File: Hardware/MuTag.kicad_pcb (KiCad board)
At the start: 2 copper layers, 58.8 x 20 mm, 30 parts, among them IC1 ST25DV04K-IER6S3, J1 SPI_Header, U2 ATTiny

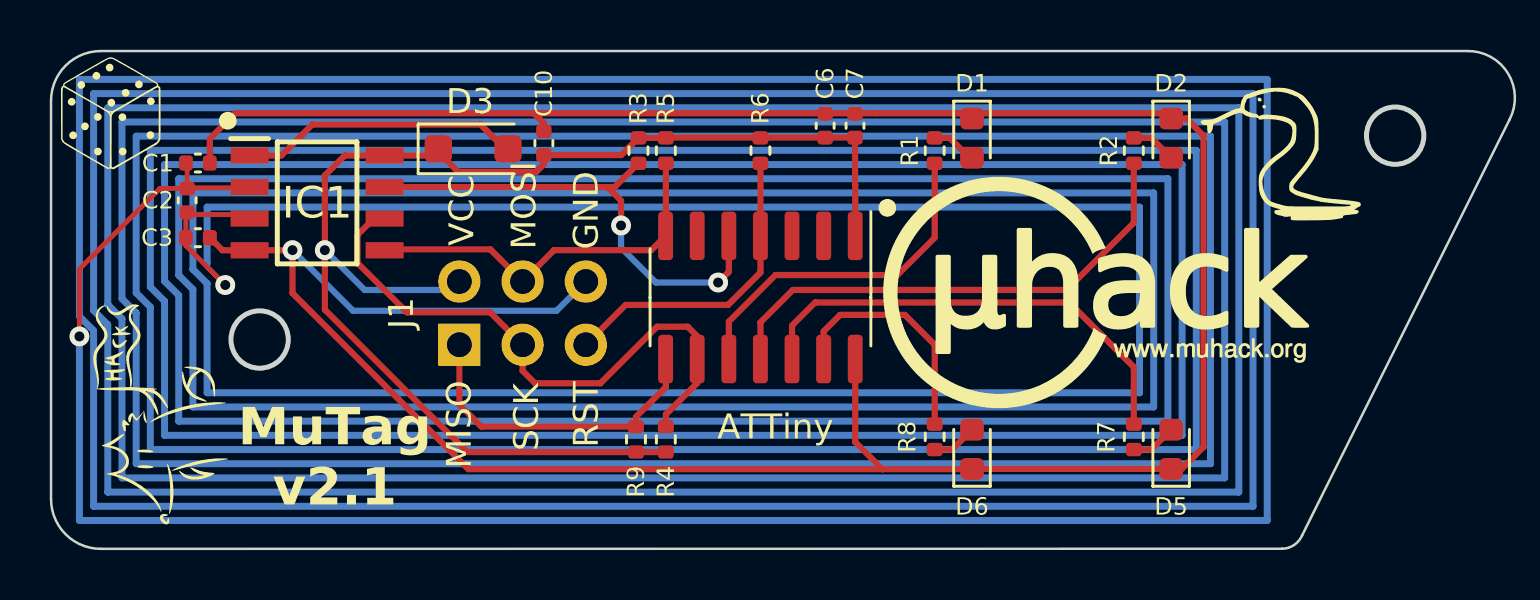
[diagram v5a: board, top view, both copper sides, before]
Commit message: Modified led resistor to 150 - increased distance between components to be hand soldered - modified graphics
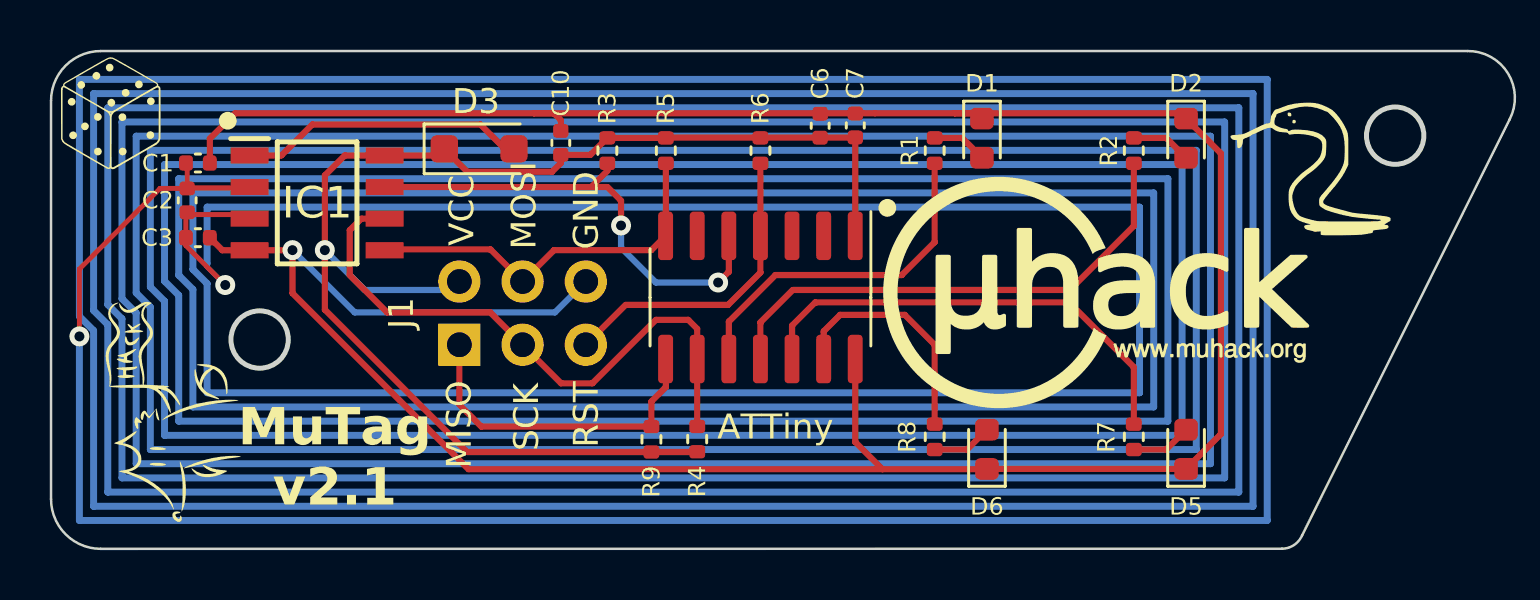
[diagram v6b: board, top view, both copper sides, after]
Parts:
- removed the G*** at (70.2, 29.8)
- removed the G*** at (49.9, 30.2)
- added G***: LOGO, LOGO, B.Cu at (70.3, 30.0)
- added G***: LOGO, LOGO, B.Cu at (44.3, 30.9)
- moved G*** 1.34 mm to (81.5, 24.5)
- moved R4 1.26 mm to (56.0, 35.6)
- moved R3 1.25 mm to (52.4, 24.0)
- moved C10 0.68 mm to (50.5, 23.7)
- moved R9 0.62 mm to (54.1, 35.6)
- moved D2 0.60 mm to (75.6, 23.5)
- moved D5 0.60 mm to (75.6, 36.0)
- moved D6 0.60 mm to (67.6, 36.0)
- moved G*** 0.51 mm to (34.9, 34.5)
- moved D1 0.40 mm to (67.4, 23.5)
- moved D3 0.24 mm to (47.2, 23.9)
- moved C6 0.20 mm to (60.9, 23.0)
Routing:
- net GND: track 119.1 -> 121.0 mm
- net VCC: track 54.6 -> 55.8 mm
- net /INT0: track 20.4 -> 19.4 mm
- net Net-(D1-A): track 1.59 -> 2.23 mm
- net Net-(D2-A): track 1.83 -> 2.43 mm
- net Net-(D6-A): track 1.83 -> 2.43 mm
- net Net-(D5-A): track 1.83 -> 2.43 mm
